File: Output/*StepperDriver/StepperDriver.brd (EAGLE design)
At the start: 20 x 13 mm, 15 parts, among them U2 DRV8834RGET

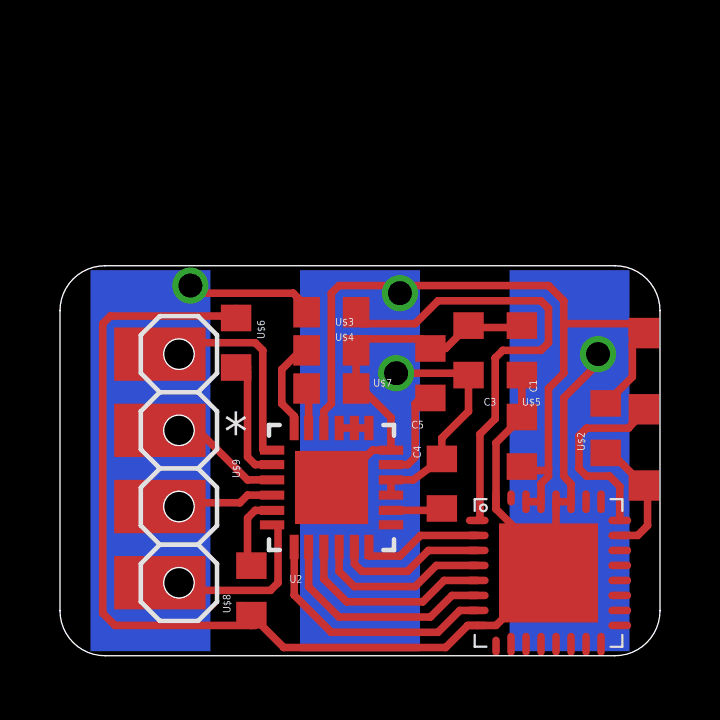
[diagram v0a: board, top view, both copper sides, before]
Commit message: Update Pinheader
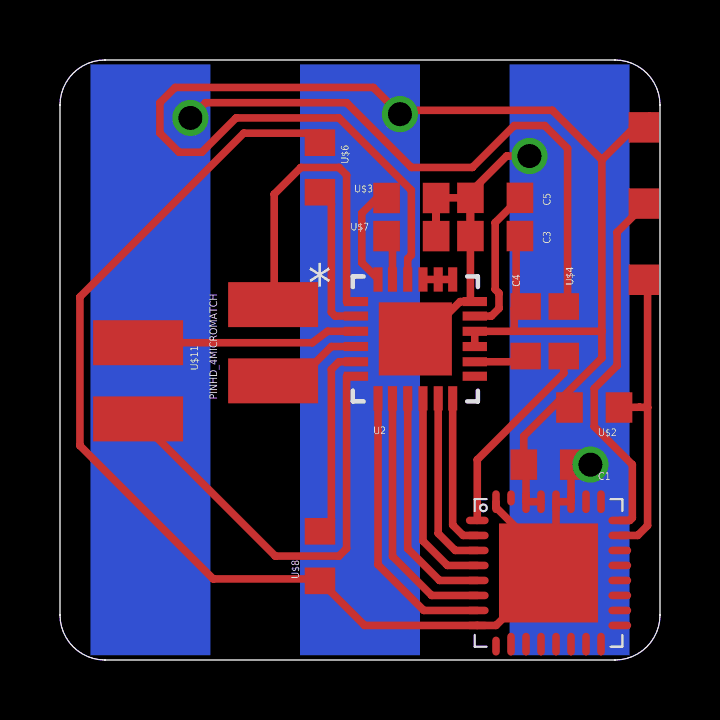
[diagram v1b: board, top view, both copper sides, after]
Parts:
- removed U$5: 0, thar:603
- removed U$9: PINHD_42.54MOD, thar:PINHD_4_MOD
- added U$11: PINHD_4MICROMATCH, thar:MICROMATCH4P0L
- U$1: value CARRIER_SMD2SMD2_3POL -> CARRIER_SMD2SMD2_3POL_W; device thar:CARRIER_SMD2_3POL -> thar:CARRIER_SMD2_WIDE_3POL
- moved U$4 7.77 mm to (18.5, 12.1), turned to 90 degrees
- moved U$1 6.86 mm to (11.8, 14.6)
- moved U$6 6.48 mm to (10.4, 17.5)
- moved C5 6.23 mm to (16.3, 16.5), turned to 0 degrees
- moved C4 5.80 mm to (17.3, 12.1)
- moved U$7 5.74 mm to (13.5, 15.2)
- moved U$3 5.74 mm to (13.5, 16.5)
- moved U2 5.69 mm to (13.6, 11.8)
- moved C3 3.91 mm to (16.3, 15.2), turned to 180 degrees
- moved U$8 2.56 mm to (10.4, 4.57)
- moved C1 1.17 mm to (18.0, 7.62), turned to 0 degrees
- moved U$2 0.79 mm to (19.6, 9.53), turned to 180 degrees
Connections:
- removed net N$21: C3.2, C5.1, U$3.1, U$5.1, U$7.1, U2.18, U2.25
- net GND: now also C3.2, C5.1, U$3.1, U$7.1, U2.18, U2.25; no longer U$5.2
- net N$16: now also U$11.P$4; no longer U$9.P$4
- net N$18: now also U$11.P$3; no longer U$9.P$3
- net N$23: now also U$11.P$1; no longer U$9.P$1
- net N$24: now also U$11.P$2; no longer U$9.P$2
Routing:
- net N$12: track 10.9 -> 32.6 mm
- net VCC: track 48.8 -> 68.1 mm, vias 2 -> 1
- net N$21: track 13.3 -> 0.00 mm
- net N$11: track 15.9 -> 6.67 mm
- net N$16: track 7.22 -> 15.0 mm
- net N$4: track 4.17 -> 10.3 mm
- net N$3: track 6.82 -> 12.1 mm
- net N$14: track 2.57 -> 6.48 mm
- net N$23: track 7.35 -> 11.1 mm
- net N$24: track 4.72 -> 7.39 mm
- net N$2: track 3.25 -> 4.99 mm
- net N$36: track 4.19 -> 5.19 mm
- net N$32: track 5.05 -> 6.04 mm
- net N$29: track 5.92 -> 6.90 mm
- net N$37: track 6.79 -> 7.77 mm
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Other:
- board size 20 x 13 mm -> 20 x 20 mm
